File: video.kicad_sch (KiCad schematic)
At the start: 22 parts, among them J2 DIN-7 Video, J3 DIN-5 Audio, J4 DIN-5 Power, J8 RGB/Composite, Q1 BC547B, Q3 BC547B, Q4 BC547B, Q5 BC547B, Q6 BC547B

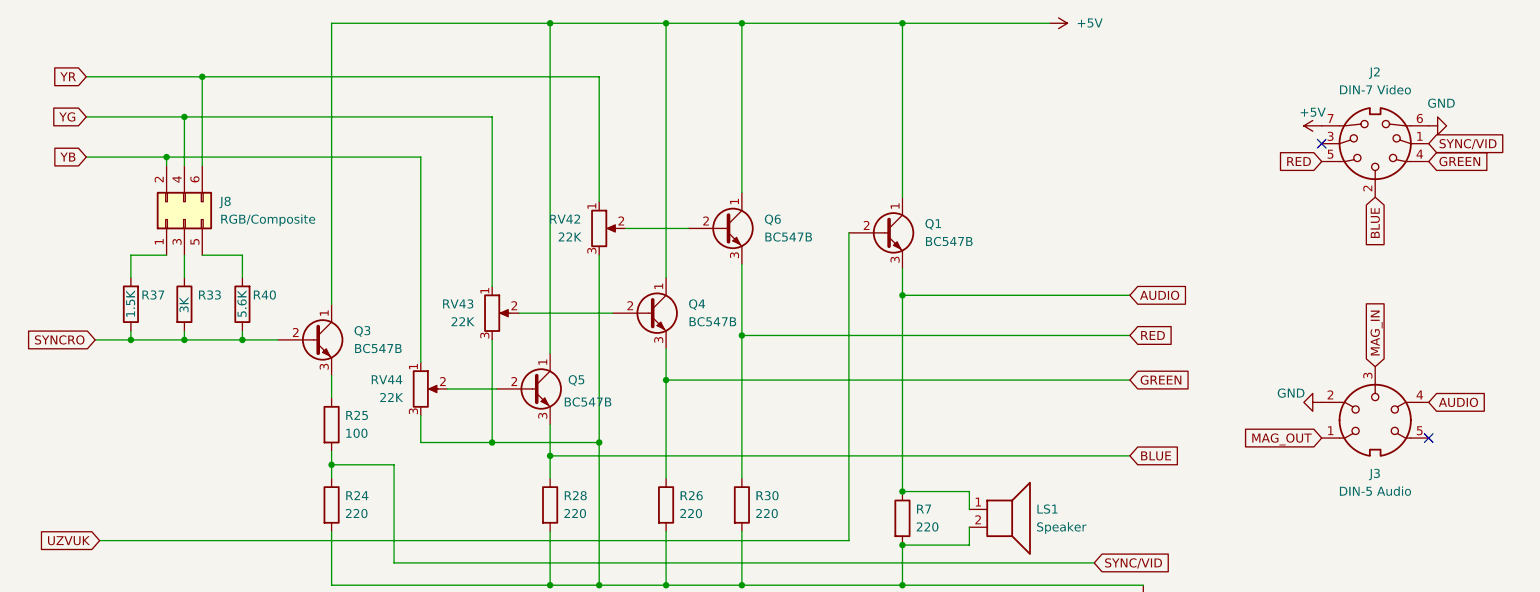
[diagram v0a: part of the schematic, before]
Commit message: Version 1.0 schematics and PCB complete
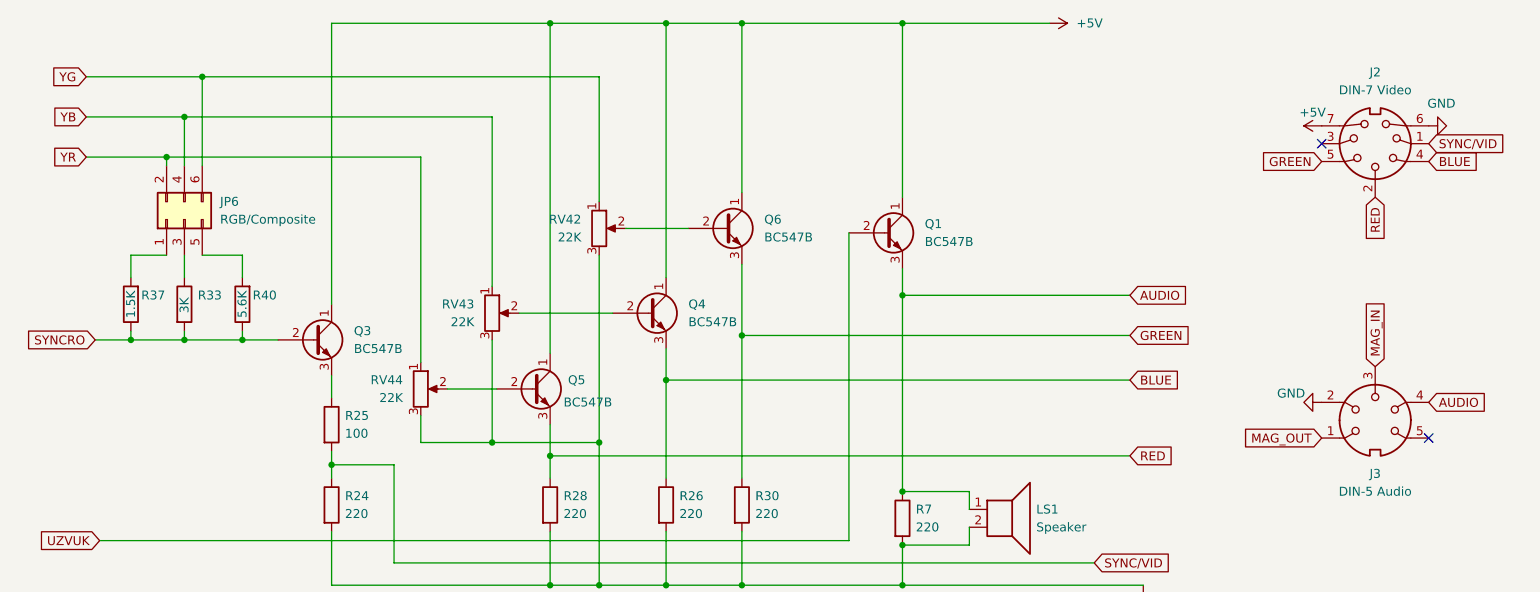
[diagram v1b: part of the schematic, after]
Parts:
- J2: symbol Connector:DIN-7 -> Delta_s_m_Lib:DIN-7
- J3, J4: symbol Connector:DIN-5 -> Delta_s_m_Lib:DIN-5
- JP6: renamed from J8; symbol Connector_Generic:Conn_02x03_Odd_Even -> Delta_s_m_Lib:Conn_02x03_Odd_Even
- LS1: footprint Connector_PinHeader_2.54mm:PinHeader_1x02_P2.54mm_Vertical -> delta:ZM-Piezo Buzzer-2207T2; symbol Device:Speaker -> Delta_s_m_Lib:Speaker
- Q1, Q3, Q4, Q5, Q6: symbol Transistor_BJT:BC547 -> Delta_s_m_Lib:BC547
- R24, R25, R26, R28, R30, R33, R37, R40, R7: symbol Device:R -> Delta_s_m_Lib:R
- RV42, RV43, RV44: symbol Device:R_Potentiometer -> Delta_s_m_Lib:R_Potentiometer
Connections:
- net BLUE: now also J2.4, Q4.3 (E), R26.1; no longer J2.2, Q5.3 (E), R28.1
- net GREEN: now also J2.5, Q6.3 (E), R30.1; no longer J2.4, Q4.3 (E), R26.1
- net RED: now also J2.2, Q5.3 (E), R28.1; no longer J2.5, Q6.3 (E), R30.1
- net YB: now also JP6.4 (Pin_4), RV43.1; no longer JP6.2 (Pin_2), RV44.1
- net YG: now also JP6.6 (Pin_6), RV42.1; no longer JP6.4 (Pin_4), RV43.1
- net YR: now also JP6.2 (Pin_2), RV44.1; no longer JP6.6 (Pin_6), RV42.1

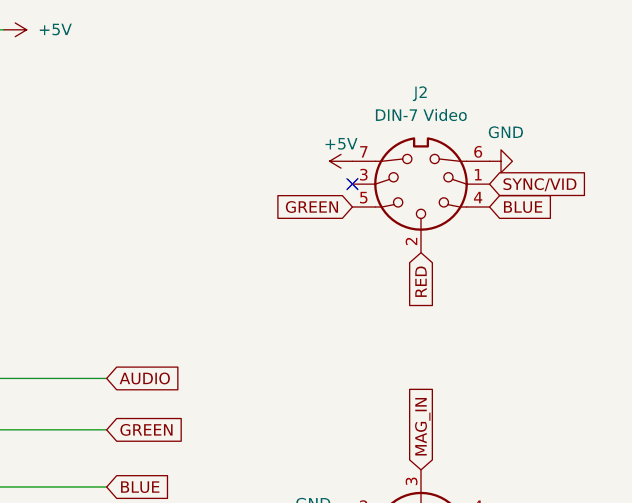
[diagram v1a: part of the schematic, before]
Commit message: Video connector fix and labels
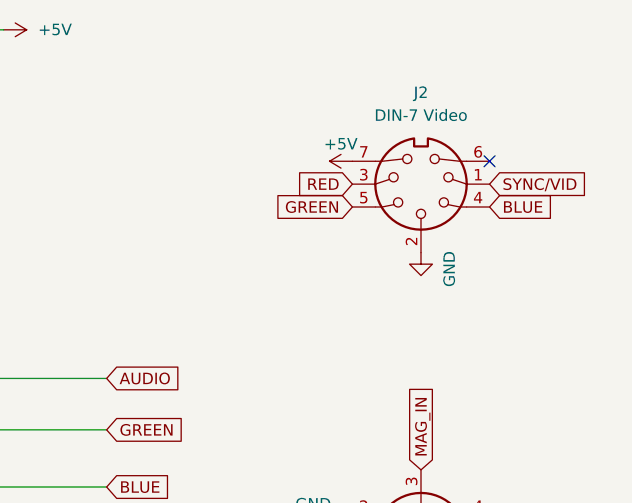
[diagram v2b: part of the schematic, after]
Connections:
- net GND: now also J2.2; no longer J2.6
- net RED: now also J2.3; no longer J2.2
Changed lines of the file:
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@@
   (junction (at 180.975 117.475) (diameter 0) (color 0 0 0 0)
   )
-  (no_connect (at 240.665 67.945))
   (no_connect (at 256.54 145.415))
   (no_connect (at 255.905 109.855))
+  (no_connect (at 255.905 65.405))
   (no_connect (at 256.54 140.335))
   (wire (pts (xy 99.695 113.665) (xy 99.695 115.57))
@@
     )
   )
-  (global_label "RED" (shape input) (at 248.285 75.565 270) (fields_autoplaced)
-    (effects (font (size 1.27 1.27)) (justify right))
-    (property "Intersheetrefs" "${INTERSHEET_REFS}" (at 248.285 82.1598 90)
-      (effects (font (size 1.27 1.27)) (justify right) hide)
-    )
-  )
   (global_label "SYNCRO" (shape input) (at 66.04 95.885 180) (fields_autoplaced)
     (effects (font (size 1.27 1.27)) (justify right))
@@
     )
   )
+  (global_label "RED" (shape input) (at 240.665 67.945 180) (fields_autoplaced)
+    (effects (font (size 1.27 1.27)) (justify right))
+    (property "Intersheetrefs" "${INTERSHEET_REFS}" (at 234.0702 67.945 0)
+      (effects (font (size 1.27 1.27)) (justify right) hide)
+    )
+  )
   (global_label "YB" (shape input) (at 64.77 64.135 180) (fields_autoplaced)
     (effects (font (size 1.27 1.27)) (justify right))
@@
         (path "/31325de8-16cf-4c6f-92cf-6f5a8aaa6830/65352eb4-688f-4c08-b5e4-ec3cc93bd7c5"
           (reference "#PWR0246") (unit 1)
+        )
+      )
+    )
+  )
+  (symbol (lib_id "power:GND") (at 248.285 75.565 0) (unit 1)
+    (in_bom yes) (on_board yes) (dnp no)
+    (property "Reference" "#PWR03" (at 248.285 81.915 0)
+      (effects (font (size 1.27 1.27)) hide)
+    )
+    (property "Value" "GND" (at 251.46 79.375 90)
+      (effects (font (size 1.27 1.27)) (justify left))
+    )
+    (property "Footprint" "" (at 248.285 75.565 0)
+      (effects (font (size 1.27 1.27)) hide)
+    )
+    (property "Datasheet" "" (at 248.285 75.565 0)
+      (effects (font (size 1.27 1.27)) hide)
+    )
+    (pin "1")
+    (instances
+      (project "delta48m"
+        (path "/31325de8-16cf-4c6f-92cf-6f5a8aaa6830/65352eb4-688f-4c08-b5e4-ec3cc93bd7c5"
+          (reference "#PWR03") (unit 1)
         )
       )
@@
         )
       )
-    )
-  )
-  (symbol (lib_id "power:GND") (at 255.905 65.405 90) (unit 1)
-    (in_bom yes) (on_board yes) (dnp no)
-    (property "Reference" "#PWR0250" (at 262.255 65.405 0)
-      (effects (font (size 1.27 1.27)) hide)
-    )
-    (property "Value" "GND" (at 259.715 62.23 90)
-      (effects (font (size 1.27 1.27)) (justify left))
-    )
-    (property "Footprint" "" (at 255.905 65.405 0)
-      (effects (font (size 1.27 1.27)) hide)
-    )
-    (property "Datasheet" "" (at 255.905 65.405 0)
-      (effects (font (size 1.27 1.27)) hide)
-    )
-    (pin "1")
-    (instances
-      (project "delta48m"
-        (path "/31325de8-16cf-4c6f-92cf-6f5a8aaa6830/65352eb4-688f-4c08-b5e4-ec3cc93bd7c5"
-          (reference "#PWR0250") (unit 1)
-        )
-      )

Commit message: Version 1.2 update
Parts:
- added J8: USB_PORT, Connector_PinHeader_2.54mm:PinHeader_1x04_P2.54mm_Vertical, symbol Connector_Generic:Conn_01x04
- J2: footprint w_conn_av:DIN-7-Variable -> Delta_sm_lib:DIN-7-Variable
- J3, J4: footprint w_conn_av:DIN-5-Variable -> Delta_sm_lib:DIN-5-Variable
- JP6: footprint Connector_PinHeader_2.54mm:PinHeader_2x03_P2.54mm_Vertical -> Delta_sm_lib:PinHeader_2x03_P2.54mm_Vertical
- LS1: footprint delta:ZM-Piezo Buzzer-2207T2 -> Delta_sm_lib:ZM-Piezo Buzzer-2207T2
- Q1, Q3, Q4, Q5, Q6: footprint Package_TO_SOT_THT:TO-92_Inline -> Delta_sm_lib:TO-92_Inline
- R24, R25, R26, R28, R30, R33, R37, R40, R7: footprint Resistor_THT:R_Axial_DIN0207_L6.3mm_D2.5mm_P10.16mm_Horizontal -> Delta_sm_lib:R_Axial_DIN0207_L6.3mm_D2.5mm_P10.16mm_Horizontal
- RV42, RV43, RV44: footprint Potentiometer_THT:Potentiometer_Bourns_3299X_Horizontal -> Delta_sm_lib:Potentiometer_Bourns_3299X_Horizontal
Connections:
- net +5V: now also J8.1 (Pin_1)
- net GND: now also J8.4 (Pin_4)
- no-connect marks 4 -> 6

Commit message: Update 1.2, additional pins
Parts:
- added J11: Conn_01x06, Connector_PinHeader_2.54mm:PinHeader_1x06_P2.54mm_Vertical, symbol Connector_Generic:Conn_01x06
- added J12: Conn_01x04, Connector_PinHeader_2.54mm:PinHeader_1x04_P2.54mm_Vertical, symbol Connector_Generic:Conn_01x04
- added J13: Conn_01x02, Connector_PinHeader_2.54mm:PinHeader_1x02_P2.54mm_Vertical, symbol Connector_Generic:Conn_01x02
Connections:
- net +5V: now also J11.6 (Pin_6)
- net AUDIO: now also J12.4 (Pin_4), J13.1 (Pin_1)
- net BLUE: now also J11.4 (Pin_4)
- net GND: now also J11.2 (Pin_2), J12.2 (Pin_2), J13.2 (Pin_2)
- net GREEN: now also J11.5 (Pin_5)
- net MAG_IN: now also J12.3 (Pin_3)
- net MAG_OUT: now also J12.1 (Pin_1)
- net RED: now also J11.3 (Pin_3)
- net SYNC/VID: now also J11.1 (Pin_1)
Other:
- moved on the sheet: J3, LS1

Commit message: Topology for version 1.2
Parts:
- added LS2: 1407, Delta_sm_lib:1407 Piezoelectric Passive Buzzer, symbol Delta_s_m_Lib:Speaker
- J8: footprint Connector_PinHeader_2.54mm:PinHeader_1x04_P2.54mm_Vertical -> Delta_sm_lib:USB-C Power board
- LS1: value Speaker -> 2207
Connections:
- net AUDIO: now also LS2.1
- net GND: now also LS2.2
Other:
- moved on the sheet: J11, J12, J13, J2, J3, J4, J8, JP6, LS1, Q1, Q3, Q4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

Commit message: Fixes
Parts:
- added C7: 4.7µF 16V, Delta_sm_lib:CP_Radial_D4.0mm_P2.00mm, symbol Delta_s_m_Lib:C_Polarized
- added R17, R18, R27: 220, Delta_sm_lib:R_Axial_DIN0207_L6.3mm_D2.5mm_P10.16mm_Horizontal, symbol Delta_s_m_Lib:R
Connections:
- net AUDIO: now also J2.6, C7.1; no longer J13.1 (Pin_1), LS1.1, LS2.1, Q1.3 (E), R7.1
- net BLUE: now also J11.5 (Pin_5), J2.5, R30.1, R27.2; no longer J11.4 (Pin_4), J2.4, Q4.3 (E), R26.1
- net GREEN: now also J11.4 (Pin_4), J2.4, R28.1, R17.2; no longer J11.5 (Pin_5), J2.5, Q6.3 (E), R30.1
- net RED: now also R26.1, R18.2; no longer Q5.3 (E), R28.1
- net YB: now also JP6.6 (Pin_6), RV42.1; no longer JP6.4 (Pin_4), RV43.1
- net YG: now also JP6.2 (Pin_2), RV44.1; no longer JP6.6 (Pin_6), RV42.1
- net YR: now also JP6.4 (Pin_4), RV43.1; no longer JP6.2 (Pin_2), RV44.1
- new net: C7.2, J13.1 (Pin_1), LS1.1, LS2.1, Q1.3 (E), R7.1
- new net: Q4.3 (E), R18.1
- new net: Q6.3 (E), R27.1
- new net: Q5.3 (E), R17.1
- no-connect marks 6 -> 5
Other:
- moved on the sheet: J13, LS1, LS2, R24, R26, R28, R30, R7
